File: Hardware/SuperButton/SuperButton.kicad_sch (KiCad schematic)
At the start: 24 parts, among them J101 USBC, J102 EXT_LED, J103 ICSP, SW101 Switch, U102 ATtiny85

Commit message: Come back to this later
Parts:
- added U101: ATmega8U2-A, Package_QFP:TQFP-32_7x7mm_P0.8mm, symbol MCU_Microchip_ATmega:ATmega8U2-A
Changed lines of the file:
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@@
     (pin "1")
+  )
+  (symbol (lib_id "MCU_Microchip_ATmega:ATmega8U2-A") (at 153.67 120.65 0) (unit 1)
+    (in_bom yes) (on_board yes) (fields_autoplaced)
+    (property "Reference" "U101" (id 0) (at 155.6894 156.21 0)
+      (effects (font (size 1.27 1.27)) (justify left))
+    )
+    (property "Value" "ATmega8U2-A" (id 1) (at 155.6894 158.75 0)
+      (effects (font (size 1.27 1.27)) (justify left))
+    )
+    (property "Footprint" "Package_QFP:TQFP-32_7x7mm_P0.8mm" (id 2) (at 153.67 120.65 0)
+      (effects (font (size 1.27 1.27) italic) hide)
+    )
+    (property "Datasheet" "http://ww1.microchip.com/downloads/en/DeviceDoc/doc7799.pdf" (id 3) (at 153.67 120.65 0)
+      (effects (font (size 1.27 1.27)) hide)
+    )
+    (pin "1")
+    (pin "10")
+    (pin "11")
+    (pin "12")
+    (pin "13")
+    (pin "14")
+    (pin "15")
+    (pin "16")
+    (pin "17")
+    (pin "18")
+    (pin "19")
+    (pin "2")
+    (pin "20")
+    (pin "21")
+    (pin "22")
+    (pin "23")
+    (pin "24")
+    (pin "25")
+    (pin "26")
+    (pin "27")
+    (pin "28")
+    (pin "29")
+    (pin "3")
+    (pin "30")
+    (pin "31")
+    (pin "32")
+    (pin "4")
+    (pin "5")
+    (pin "6")
+    (pin "7")
+    (pin "8")
+    (pin "9")
   )
   (symbol (lib_id "Device:C_Small") (at 154.94 26.67 0) (unit 1)
@@
       (reference "SW101") (unit 1) (value "Switch") (footprint "Switch_Keyboard_Cherry_MX:SW_Cherry_MX_PCB")
     )
+    (path "/3d12e3a4-0875-4204-92ad-fb02d334b84e"
+      (reference "U101") (unit 1) (value "ATmega8U2-A") (footprint "Package_QFP:TQFP-32_7x7mm_P0.8mm")
+    )
     (path "/5c86ccdf-387a-4c62-808d-d2fc9b338567"

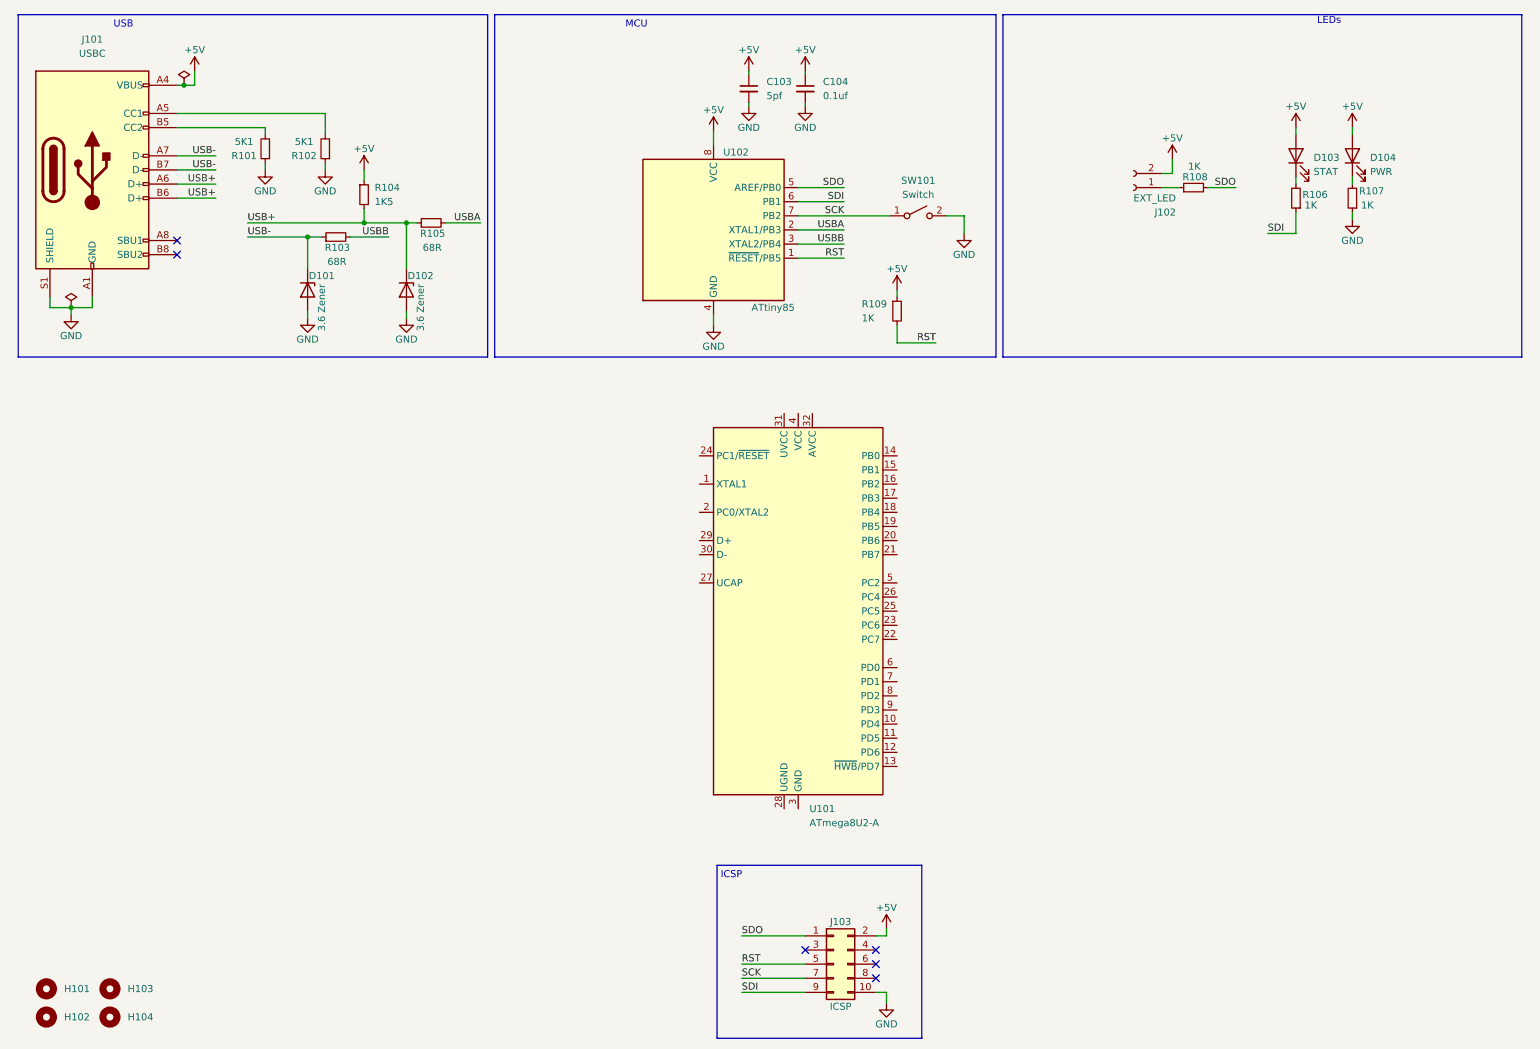
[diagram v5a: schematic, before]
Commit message: Finalize inital button design
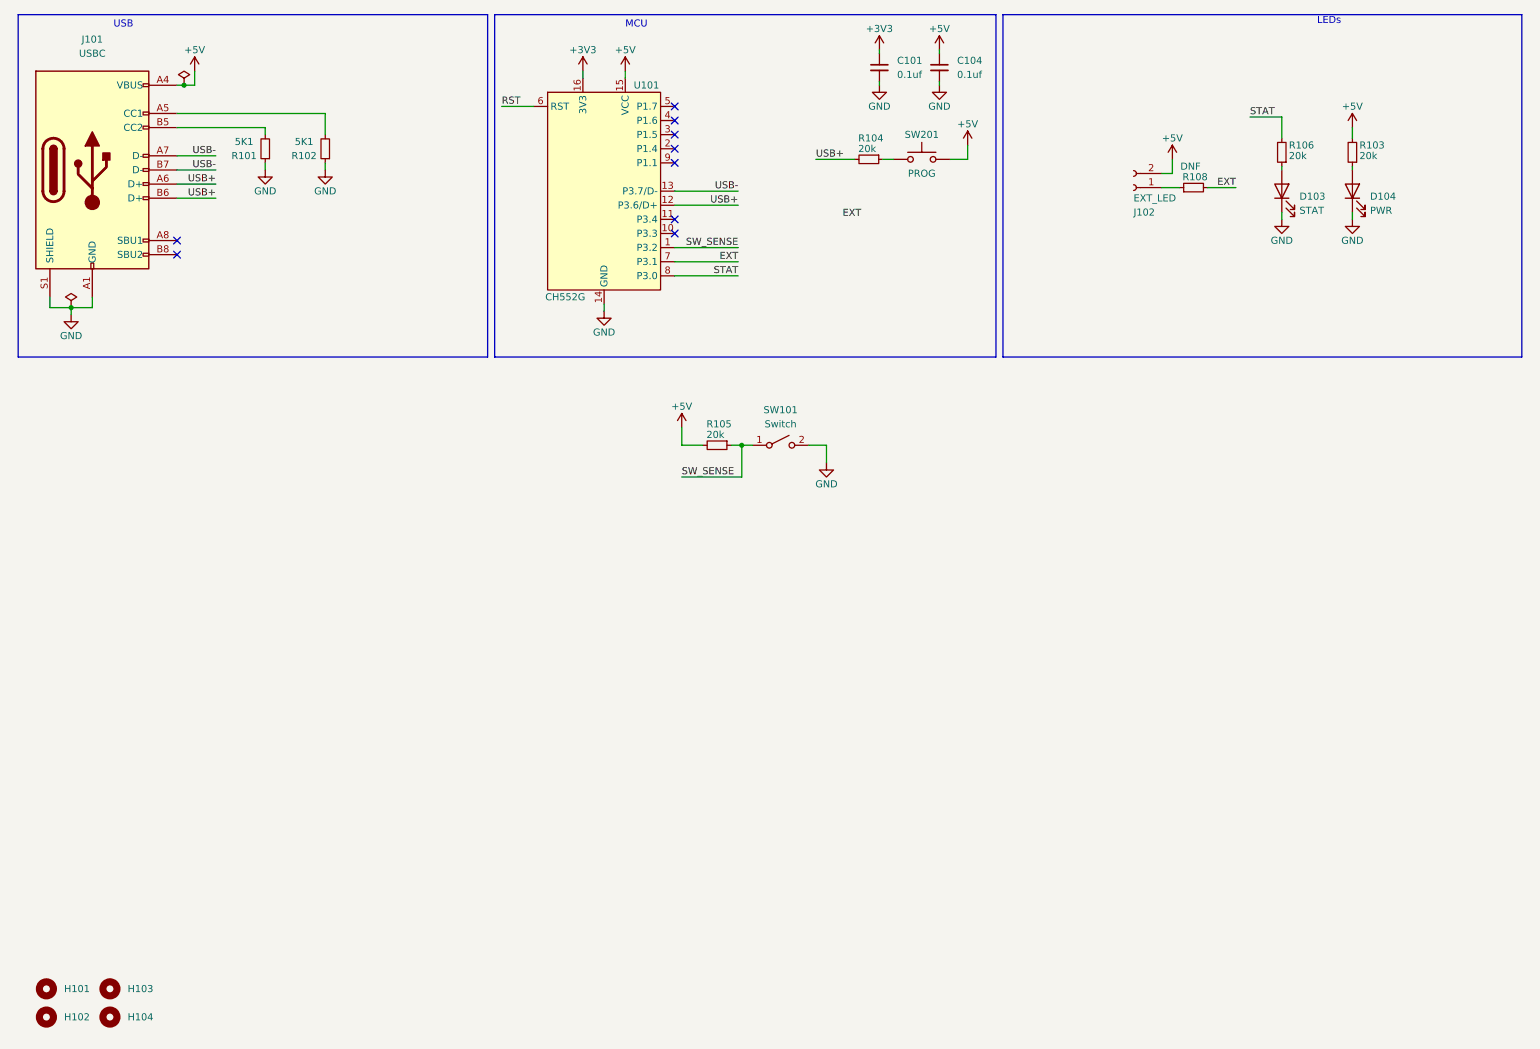
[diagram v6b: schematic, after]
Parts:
- removed C103: 5pf, Capacitor_SMD:C_0805_2012Metric, symbol Device:C_Small
- removed D101, D102: 3.6 Zener, Diode_SMD:D_0805_2012Metric, symbol Device:D_Zener
- removed J103: ICSP, Connector:Tag-Connect_TC2050-IDC-FP_2x05_P1.27mm_Vertical, symbol Connector_Generic:Conn_02x05_Odd_Even
- removed R107, R109: 1K, Resistor_SMD:R_0805_2012Metric, symbol Device:R_Small
- removed U101: ATmega8U2-A, Package_QFP:TQFP-32_7x7mm_P0.8mm, symbol MCU_Microchip_ATmega:ATmega8U2-A
- removed U102: ATtiny85, Package_SO:SOIC-8W_5.3x5.3mm_P1.27mm, symbol MCU_Microchip_ATtiny:ATtiny85-20S
- added C101: 0.1uf, Capacitor_SMD:C_0805_2012Metric, symbol Device:C_Small
- added SW201: PROG, Button_Switch_SMD:SW_SPST_TL3342, symbol Switch:SW_Push
- added U101: CH552G, Package_SO:SOP-16_3.9x9.9mm_P1.27mm, symbol KenwoodFox:CH552G
- R103, R105: value 68R -> 20k
- R104: value 1K5 -> 20k
- R106: value 1K -> 20k
- R108: value 1K -> DNF
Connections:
- net USBA is gone; now on net +5V: R105.2
- net USBB is gone; now on net +5V: R103.2
- net +5V: now also SW201.2, U101.15 (VCC); no longer D103.2 (A), D104.2 (A), R104.1
- net GND: now also D103.1 (K), D104.1 (K), C101.2, U101.14 (GND)
- net RST: now also U101.6 (RST)
- net USB+: now also U101.12 (P3.6/D+); no longer R105.1
- net USB-: now also U101.13 (P3.7/D-); no longer R103.1
- net STAT: now reaches R106.2
- net STAT: now also U101.8 (P3.0); no longer D103.1 (K)
- net SCK renamed SW_SENSE
- net SW_SENSE: now also R105.1, U101.1 (P3.2)
- net SDI: no longer names the net of R106.1
- net SDI: now also D103.2 (A)
- net SDO renamed EXT
- net EXT: now also U101.7 (P3.1)
- new net: R104.1, SW201.1
- new net: D104.2 (A), R103.1
- new net +3V3: C101.1, U101.16 (3V3)
- no-connect marks 6 -> 9
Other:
- note removed: "ICSP"
- moved on the sheet: C104, D103, D104, R106, SW101

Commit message: fixups
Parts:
- removed J102: EXT_LED, Connector_Wire:SolderWire-0.15sqmm_1x02_P4mm_D0.5mm_OD1.5mm_Relief, symbol Connector:Conn_01x02_Female
- added J103: EXT_LED, Connector_Wire:SolderWire-0.15sqmm_1x02_P4mm_D0.5mm_OD1.5mm_Relief, symbol Connector:Conn_01x02_Socket
- added TP101: TestPoint, TestPoint:TestPoint_Pad_2.5x2.5mm, symbol Connector:TestPoint
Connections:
- net +5V: now also J103.2 (Pin_2)
- net RST: now also TP101.1
- net at R108.1: now also J103.1 (Pin_1)
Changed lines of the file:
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@@
   (junction (at 43.18 26.035) (diameter 0) (color 0 0 0 0)
+  )
+  (junction (at 104.775 29.845) (diameter 0) (color 0 0 0 0)
   )
   (junction (at 22.86 66.04) (diameter 0) (color 0 0 0 0)
@@
     (stroke (width 0) (type default))
   )
+  (wire (pts (xy 104.775 29.845) (xy 106.045 29.845))
+    (stroke (width 0) (type default))
+  )
   (polyline (pts (xy 283.845 74.93) (xy 190.5 74.93))
     (stroke (width 0) (type default))
@@
     (stroke (width 0) (type default))
   )
-  (wire (pts (xy 100.33 29.845) (xy 106.045 29.845))
+  (wire (pts (xy 100.33 29.845) (xy 104.775 29.845))
     (stroke (width 0) (type default))
   )
@@
   )
   (label "USB-" (at 142.875 45.085 180) (fields_autoplaced)
-    (effects (font (size 1.27 1.27)) (justify right bottom))
-  )
-  (label "EXT" (at 165.0068 50.0327 180) (fields_autoplaced)
     (effects (font (size 1.27 1.27)) (justify right bottom))
   )
@@
         (path "/e51b0d47-7e88-4bbf-adc2-21abe8ab62c1"
           (reference "R101") (unit 1)
+        )
+      )
+    )
+  )
+  (symbol (lib_id "Connector:TestPoint") (at 104.775 29.845 0) (unit 1)
+    (in_bom yes) (on_board yes) (dnp no)
+    (property "Reference" "TP101" (at 101.6 24.765 0)
+      (effects (font (size 1.27 1.27)) (justify left))
+    )
+    (property "Value" "TestPoint" (at 100.33 29.845 0)
+      (effects (font (size 1.27 1.27)) (justify left) hide)
+    )
+    (property "Footprint" "TestPoint:TestPoint_Pad_2.5x2.5mm" (at 109.855 29.845 0)
+      (effects (font (size 1.27 1.27)) hide)
+    )
+    (property "Datasheet" "~" (at 109.855 29.845 0)
+      (effects (font (size 1.27 1.27)) hide)
+    )
+    (pin "1")
+    (instances
+      (project "SuperButton"
+        (path "/e51b0d47-7e88-4bbf-adc2-21abe8ab62c1"
+          (reference "TP101") (unit 1)
         )
       )
@@
     )
   )
+  (symbol (lib_id "Connector:Conn_01x02_Socket") (at 213.995 44.45 180) (unit 1)
+    (in_bom yes) (on_board yes) (dnp no)
+    (property "Reference" "J103" (at 214.63 46.99 0)
+      (effects (font (size 1.27 1.27)))
+    )
+    (property "Value" "EXT_LED" (at 214.63 49.53 0)
+      (effects (font (size 1.27 1.27)))
+    )
+    (property "Footprint" "Connector_Wire:SolderWire-0.15sqmm_1x02_P4mm_D0.5mm_OD1.5mm_Relief" (at 213.995 44.45 0)
+      (effects (font (size 1.27 1.27)) hide)
+    )
+    (property "Datasheet" "~" (at 213.995 44.45 0)
+      (effects (font (size 1.27 1.27)) hide)
+    )
+    (pin "1")
+    (pin "2")
+    (instances
+      (project "SuperButton"
+        (path "/e51b0d47-7e88-4bbf-adc2-21abe8ab62c1"
+          (reference "J103") (unit 1)
+        )
+      )
+    )
+  )
   (symbol (lib_id "Mechanical:MountingHole") (at 29.845 188.595 0) (unit 1)
     (in_bom yes) (on_board yes) (dnp no) (fields_autoplaced)
@@
         )
       )
-    )
-  )
-  (symbol (lib_id "Connector:Conn_01x02_Female") (at 213.995 44.45 180) (unit 1)
-    (in_bom yes) (on_board yes) (dnp no)
-    (property "Reference" "J102" (at 213.995 48.895 0)
-      (effects (font (size 1.27 1.27)) (justify right))
-    )
-    (property "Value" "EXT_LED" (at 213.995 46.355 0)
-      (effects (font (size 1.27 1.27)) (justify right))
-    )
-    (property "Footprint" "Connector_Wire:SolderWire-0.15sqmm_1x02_P4mm_D0.5mm_OD1.5mm_Relief" (at 213.995 44.45 0)
-      (effects (font (size 1.27 1.27)) hide)
-    )
-    (property "Datasheet" "~" (at 213.995 44.45 0)
-      (effects (font (size 1.27 1.27)) hide)
-    )
-    (pin "1")
-    (pin "2")
-    (instances
-      (project "SuperButton"
-        (path "/e51b0d47-7e88-4bbf-adc2-21abe8ab62c1"
-          (reference "J102") (unit 1)
-        )
-      )

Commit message: ERC
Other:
- moved on the sheet: D103, D104, J103, R103, R105, R106, R108, SW101
